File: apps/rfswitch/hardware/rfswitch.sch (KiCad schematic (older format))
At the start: 20 parts, among them J1 CONN_AC, J2 CONN_O1, J3 CONN_AC_SW1, Q1 Q_NPN_BEC, U1 HLK-PM01, U2 6N138, U3 G3MB-202P-5V, U6 TINY328

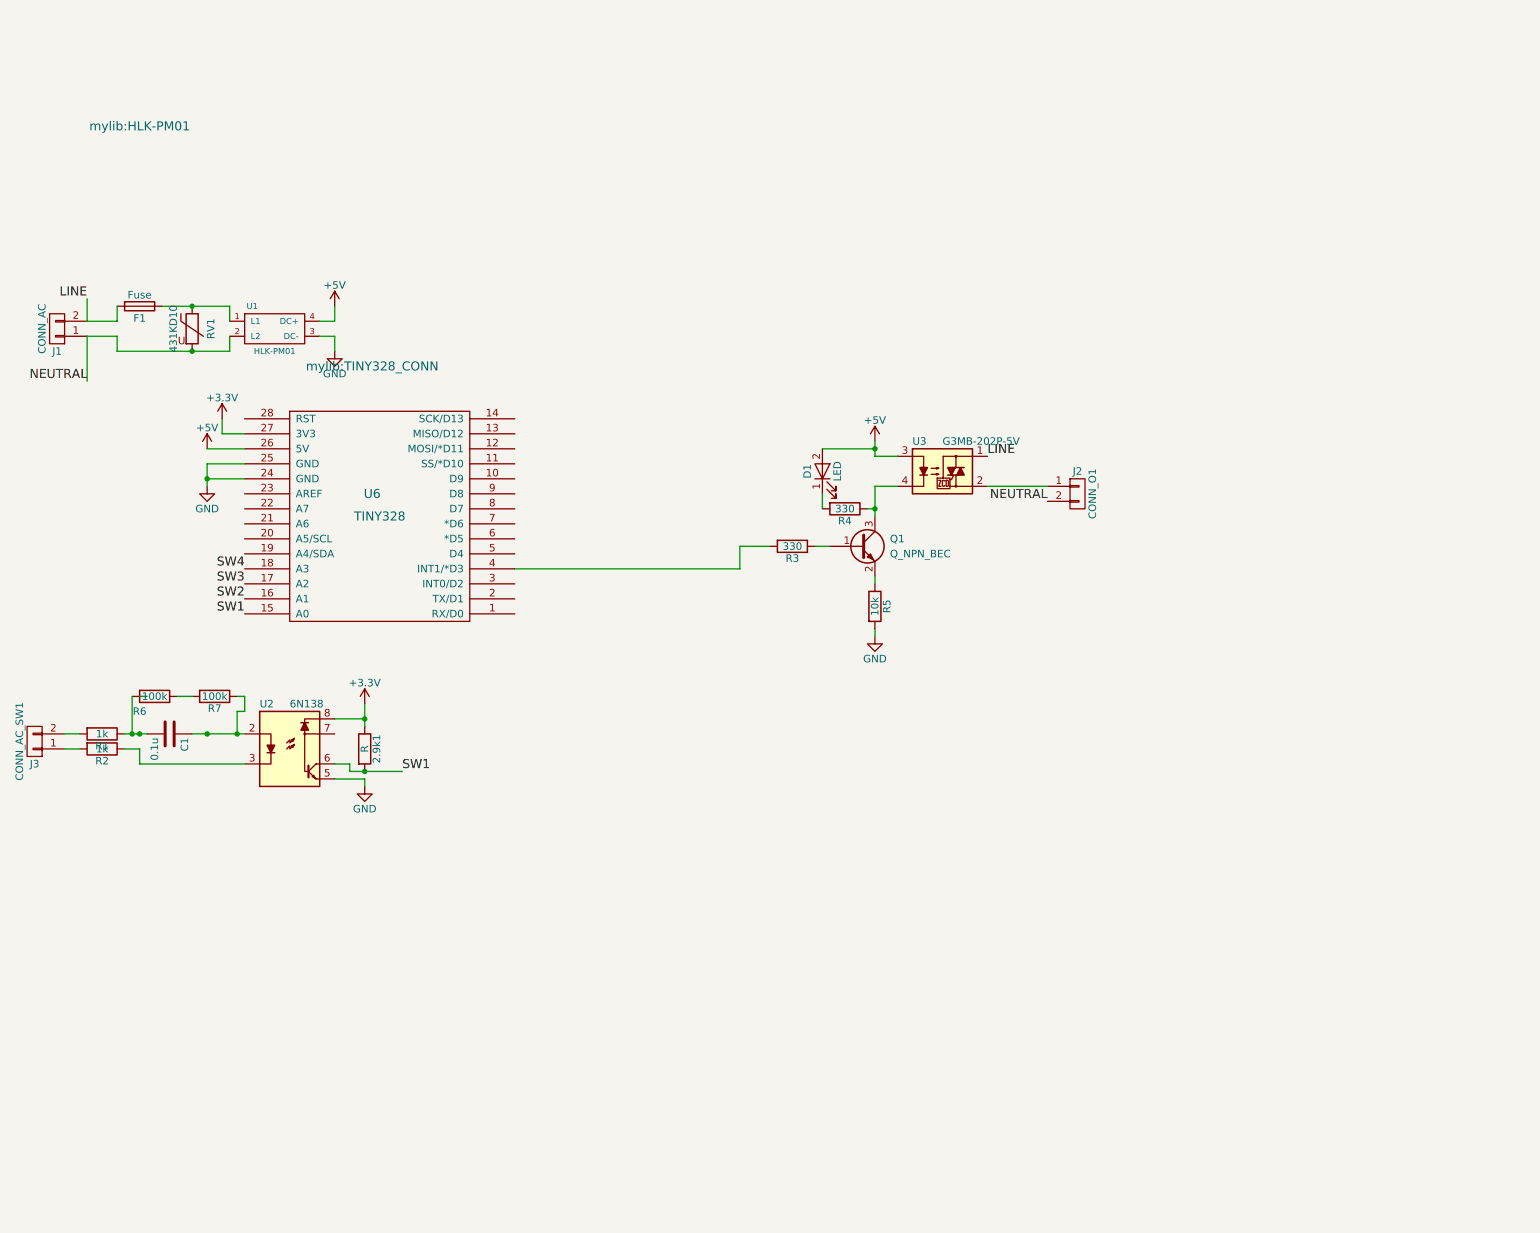
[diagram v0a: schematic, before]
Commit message: Up layout to 3 channels
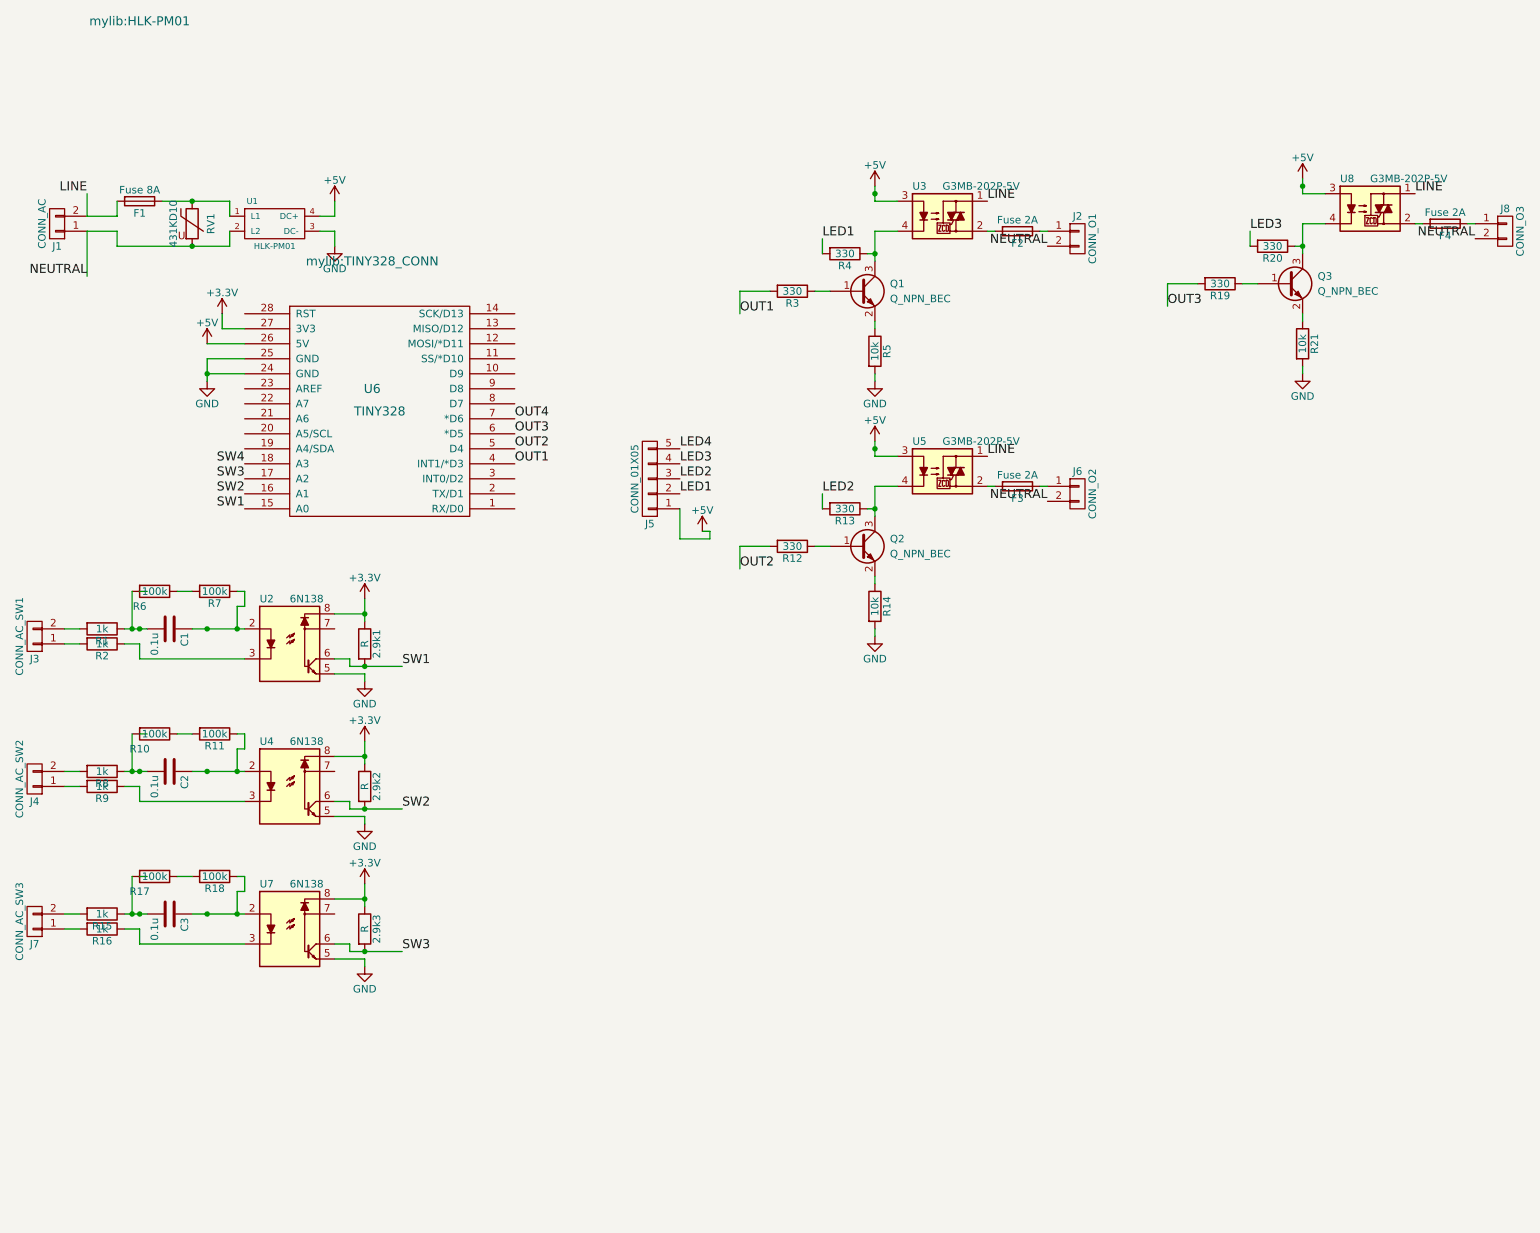
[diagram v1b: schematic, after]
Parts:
- removed D1: LED, Pin_Headers:Pin_Header_Straight_1x02_Pitch2.54mm, symbol LED
- added 2.9k2, 2.9k3: R, Resistors_SMD:R_0603_HandSoldering, symbol R
- added C2, C3: 0.1u, mylib:C_Rect_L16.5mm_W6mm_P15.00mm_MKT, symbol C
- added F2, F3, F4: Fuse 2A, Fuse_Holders_and_Fuses:Fuseholder5x20_horiz_SemiClosed_Casing10x25mm, symbol Fuse
- added J4: CONN_AC_SW2, mylib:SCREW_CONN_5mm_1x2, symbol CONN_01X02
- added J5: CONN_01X05, Pin_Headers:Pin_Header_Straight_1x05_Pitch2.54mm, symbol CONN_01X05
- added J6: CONN_O2, mylib:SCREW_CONN_5mm_1x2, symbol CONN_01X02
- added J7: CONN_AC_SW3, mylib:SCREW_CONN_5mm_1x2, symbol CONN_01X02
- added J8: CONN_O3, mylib:SCREW_CONN_5mm_1x2, symbol CONN_01X02
- added Q2, Q3: Q_NPN_BEC, TO_SOT_Packages_SMD:SOT-23, symbol Q_NPN_BEC
- added R10, R11, R17, R18: 100k, Resistors_THT:R_Axial_DIN0309_L9.0mm_D3.2mm_P12.70mm_Horizontal, symbol R
- added R12, R13, R19, R20: 330, Resistors_SMD:R_0603_HandSoldering, symbol R
- added R14, R21: 10k, Resistors_SMD:R_0603_HandSoldering, symbol R
- added R15, R16, R8, R9: 1k, Resistors_SMD:R_0603_HandSoldering, symbol R
- added U4, U7: 6N138, Housings_DIP:DIP-8_W7.62mm, symbol 6N136
- added U5, U8: G3MB-202P-5V, Housings_SIP:SIP4_Sharp-SSR_Pitch7.62mm_Straight, symbol S102S02
- C1: footprint Capacitors_THT:C_Rect_L16.5mm_W10.7mm_P15.00mm_MKT -> mylib:C_Rect_L16.5mm_W6mm_P15.00mm_MKT
- F1: value Fuse -> Fuse 8A
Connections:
- net labels added: LED1, LED2, LED3, LED4, OUT1, OUT2, OUT3, OUT4
- wire segments 55 -> 126
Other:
- moved on the sheet: 2.9k1, C1, F1, J1, J2, J3, Q1, R1, R2, R3, R4, R5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

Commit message: Adjust footprints of AC connectors to measured sizes
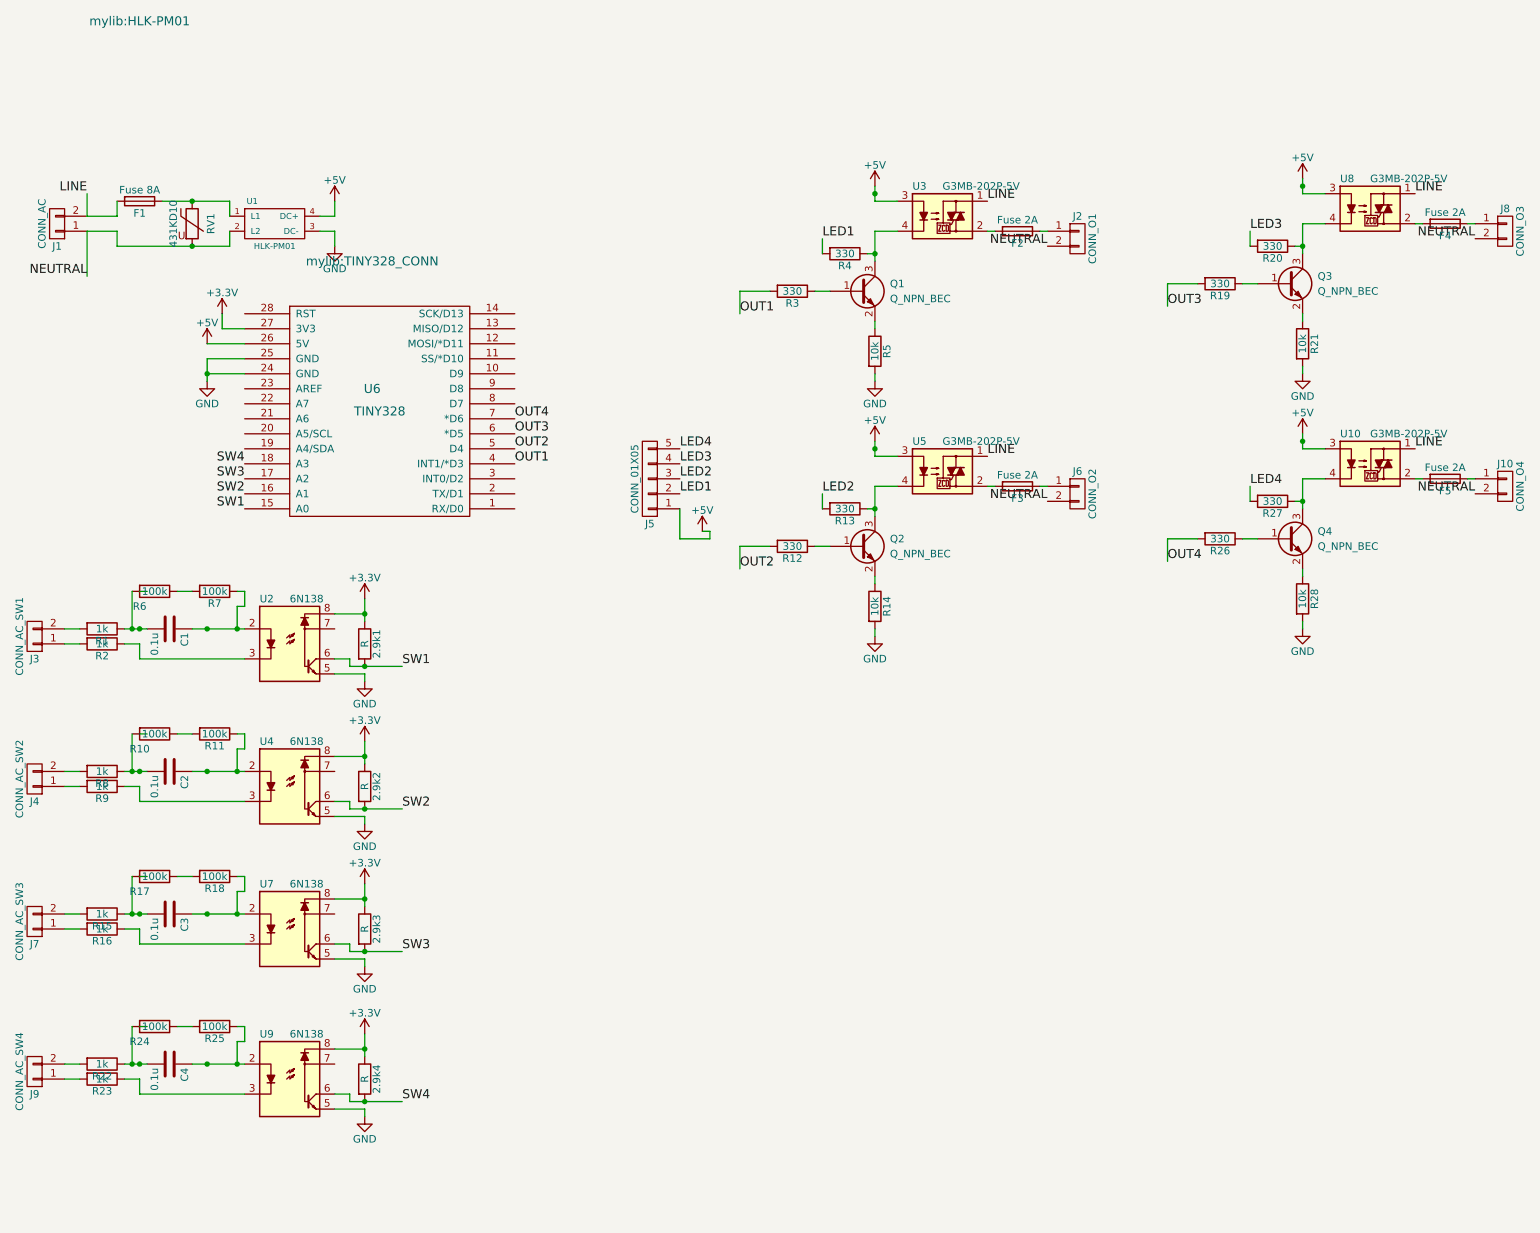
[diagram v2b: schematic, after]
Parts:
- added 2.9k4: R, Resistors_SMD:R_0603_HandSoldering, symbol R
- added C4: 0.1u, mylib:C_Rect_L16.5mm_W6mm_P15.00mm_MKT, symbol C
- added F5: Fuse 2A, Fuse_Holders_and_Fuses:Fuseholder5x20_horiz_SemiClosed_Casing10x25mm, symbol Fuse
- added J10: CONN_O4, mylib:SCREW_CONN_5mm_1x2, symbol CONN_01X02
- added J9: CONN_AC_SW4, mylib:SCREW_CONN_5mm_1x2, symbol CONN_01X02
- added Q4: Q_NPN_BEC, TO_SOT_Packages_SMD:SOT-23, symbol Q_NPN_BEC
- added R22, R23: 1k, Resistors_SMD:R_0603_HandSoldering, symbol R
- added R24, R25: 100k, Resistors_THT:R_Axial_DIN0309_L9.0mm_D3.2mm_P12.70mm_Horizontal, symbol R
- added R26, R27: 330, Resistors_SMD:R_0603_HandSoldering, symbol R
- added R28: 10k, Resistors_SMD:R_0603_HandSoldering, symbol R
- added U10: G3MB-202P-5V, Housings_SIP:SIP4_Sharp-SSR_Pitch7.62mm_Straight, symbol S102S02
- added U9: 6N138, Housings_DIP:DIP-8_W7.62mm, symbol 6N136
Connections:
- wire segments 126 -> 160

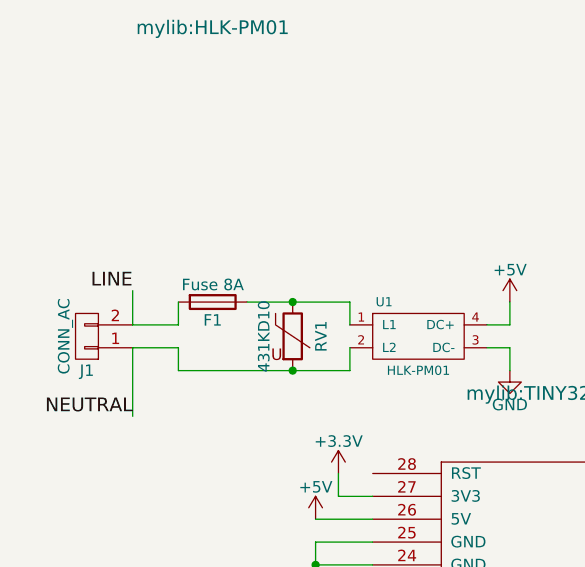
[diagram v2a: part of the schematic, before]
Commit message: Main fuse should be in line with everything. Started routing.
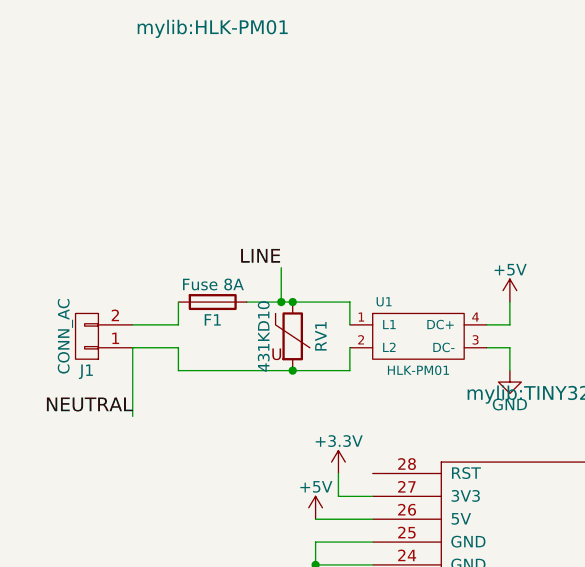
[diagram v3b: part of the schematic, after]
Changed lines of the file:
@@
 Wire Wire Line
 	5500 1700 5700 1700
-Text Label 1150 1050 2    60   ~ 0
+Text Label 1800 950  2    60   ~ 0
 LINE
-Wire Wire Line
-	1150 1050 1150 1200
 Text Label 1150 1600 2    60   ~ 0
 NEUTRAL
@@
 Wire Wire Line
 	10050 2950 10000 2950
+Wire Wire Line
+	1800 950  1800 1100
+Connection ~ 1800 1100
 $EndSCHEMATC

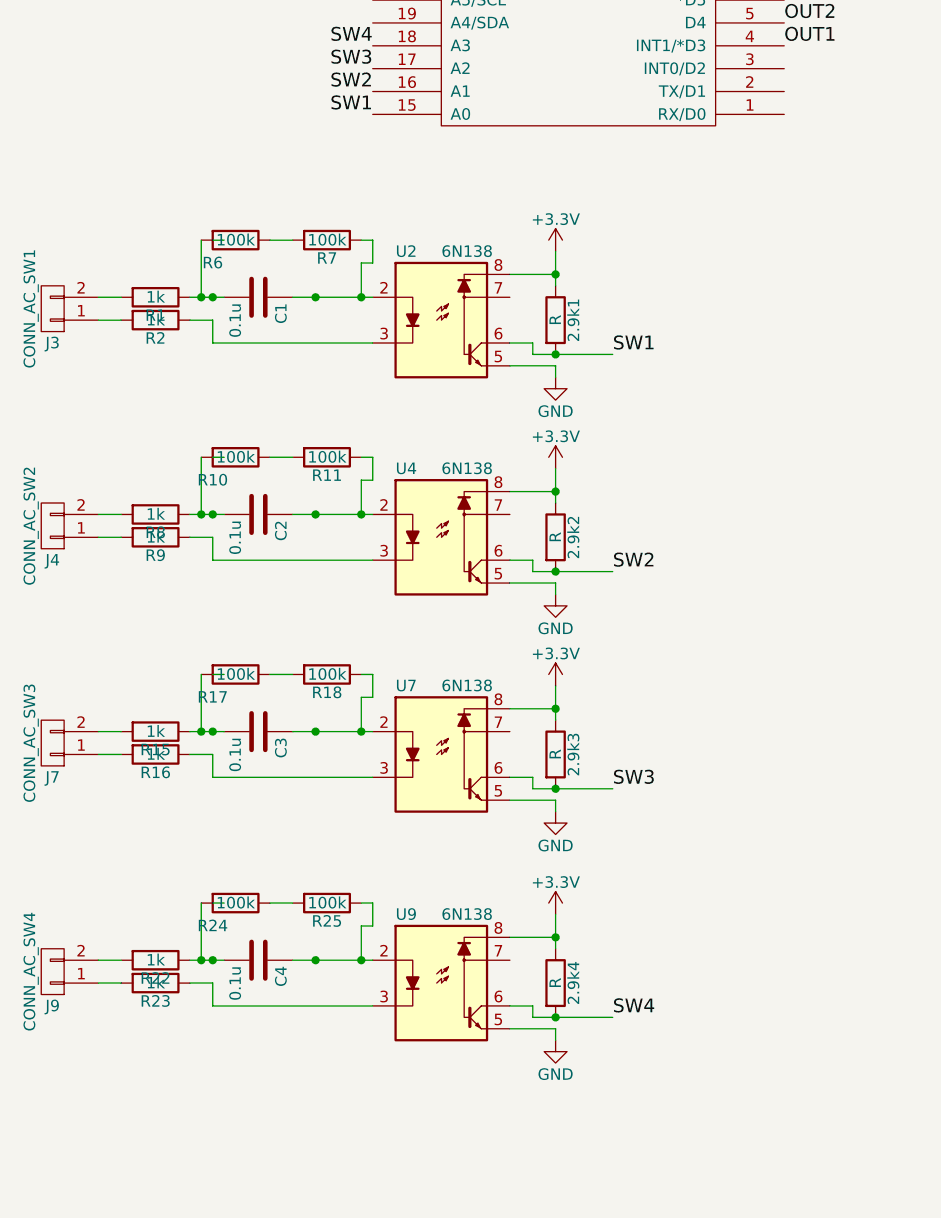
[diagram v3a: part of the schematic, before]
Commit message: Switch to quad optocoupler, almost lay-out board finished.
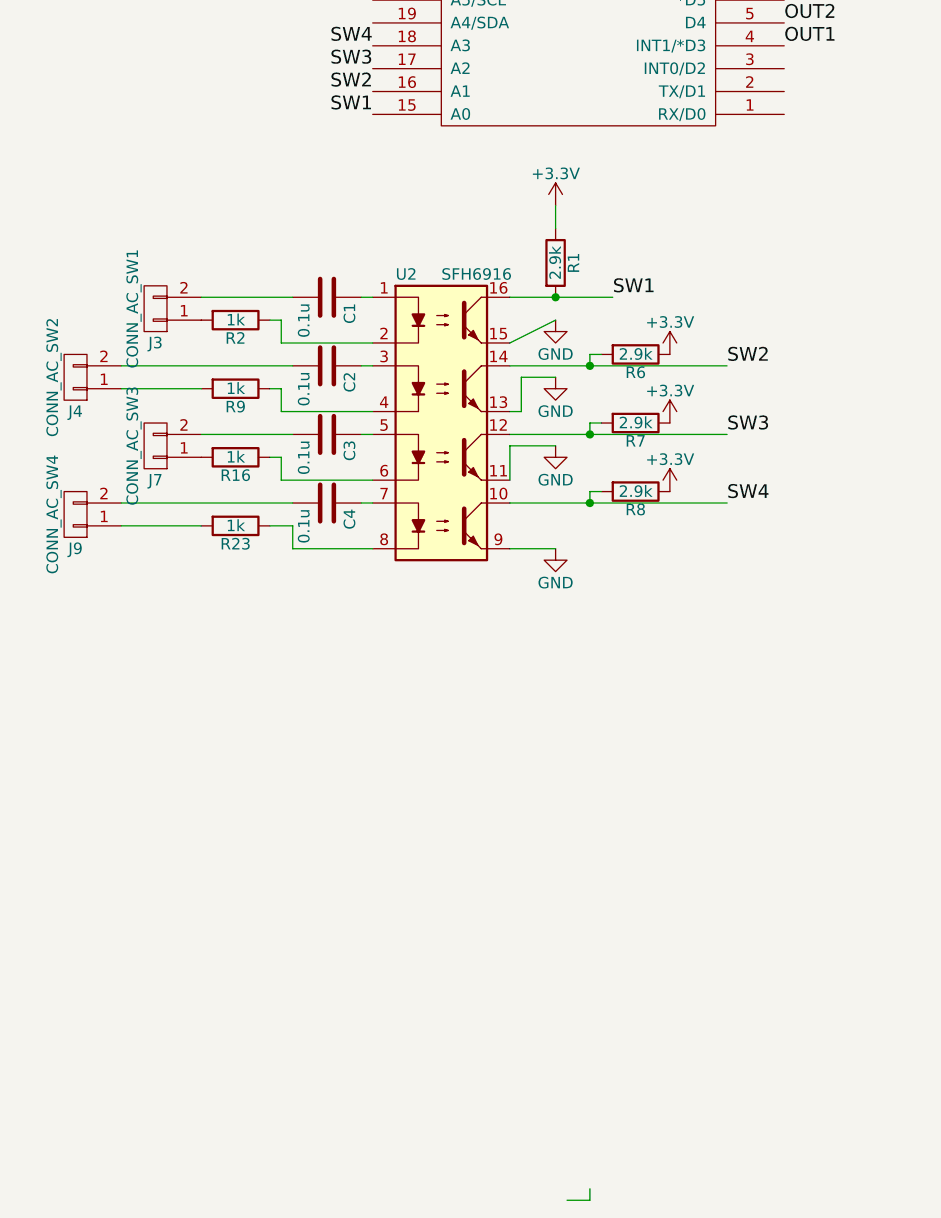
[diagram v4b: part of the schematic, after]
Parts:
- removed R1, R15, R22, R8: 1k, Resistors_SMD:R_0603_HandSoldering, symbol R
- removed R10, R11, R17, R18, R24, R25, R6, R7: 100k, Resistors_THT:R_Axial_DIN0309_L9.0mm_D3.2mm_P12.70mm_Horizontal, symbol R
- removed U2, U4, U7, U9: 6N138, Housings_DIP:DIP-8_W7.62mm, symbol 6N136
- added U2: SFH6916, Housings_SSOP:SOP-16_4.4x10.4mm_Pitch1.27mm, symbol LTV-847
- R1: renamed from 2.9k1; value R -> 2.9k
- R6: renamed from 2.9k2; value R -> 2.9k
- R7: renamed from 2.9k3; value R -> 2.9k
- R8: renamed from 2.9k4; value R -> 2.9k
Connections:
- wire segments 160 -> 118
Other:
- moved on the sheet: C1, C2, C3, C4, J3, J4, J7, J9, R1, R16, R2, R23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
